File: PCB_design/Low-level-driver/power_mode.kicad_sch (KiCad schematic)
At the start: 7 parts, among them Q401 Q_NPN_EBC, Q402 Q_NPN_EBC, U401 TMUX1204DQAR

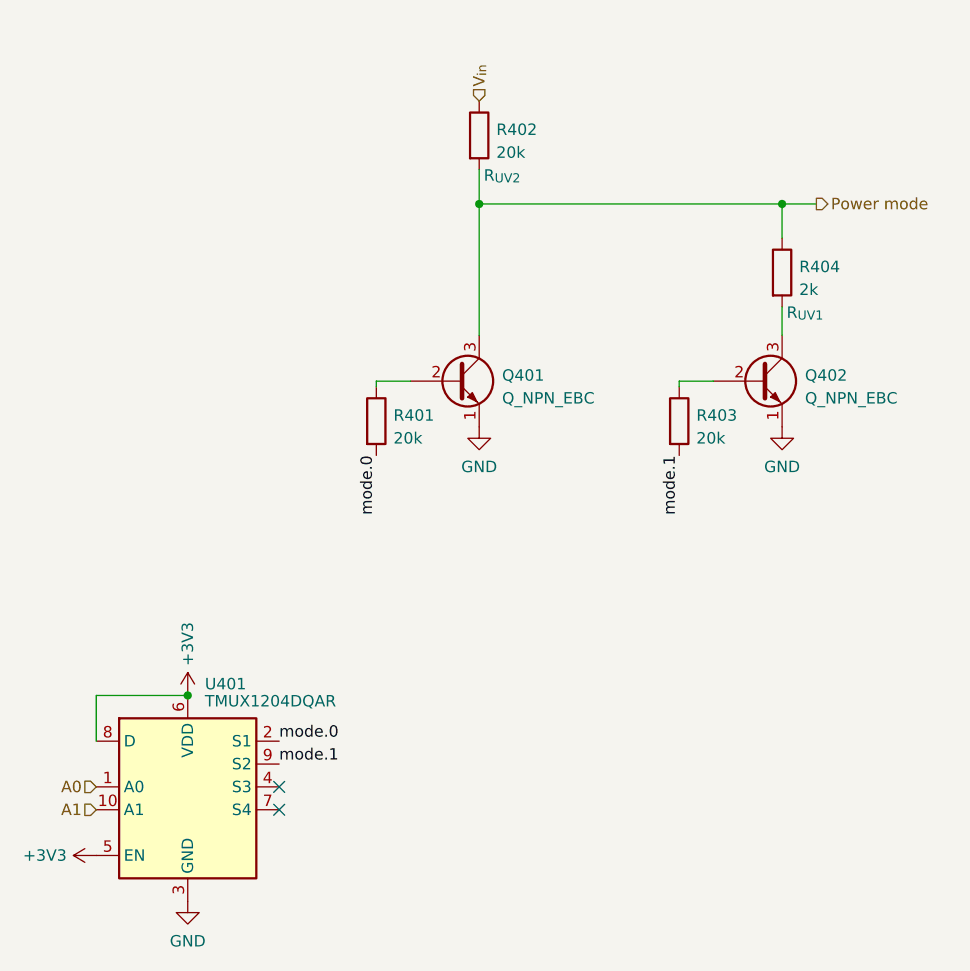
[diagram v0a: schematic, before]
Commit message: Schematic hierarchical redesign
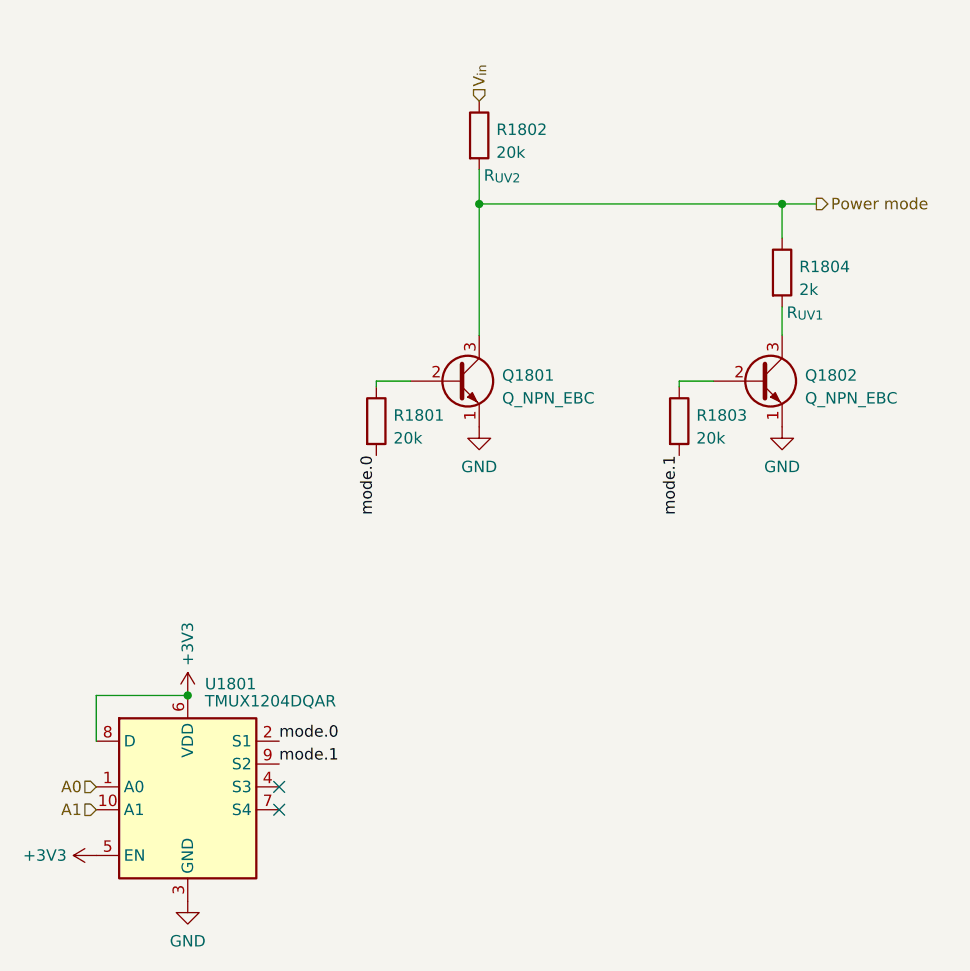
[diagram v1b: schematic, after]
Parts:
- renumbered Q401 to Q1801, Q402 to Q1802, R401 to R1801, R402 to R1802, R403 to R1803, R404 to R1804, U401 to U1801
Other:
- title: (none) -> Power supply - low level driver
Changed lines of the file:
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@@
 	(generator_version "8.0")
 	(paper "A3")
+	(title_block
+		(title "Power supply - low level driver")
+		(date "2024-06-28")
+	)
 	(junction
 		(at 118.745 68.58)
@@
 		(dnp no)
 		(fields_autoplaced yes)
-		(property "Reference" "Q402"
+		(property "Reference" "Q1802"
 			(at 154.94 87.63 0)
 			(effects
@@
 			(project "Low-level-driver"
 				(path "/2e43a8c9-1b23-4896-a481-133b23afb346/01ca3785-0e3e-4a04-8db2-6c3c91b7e708/0f5f3a01-f1db-43da-b53b-d3878d37b104"
-					(reference "Q402")
+					(reference "Q1802")
 					(unit 1)
 				)
@@
 		(on_board yes)
 		(dnp no)
-		(property "Reference" "#PWR0401"
+		(property "Reference" "#PWR01801"
 			(at 80.01 140.97 0)
 			(effects
@@
 			(project "Low-level-driver"
 				(path "/2e43a8c9-1b23-4896-a481-133b23afb346/01ca3785-0e3e-4a04-8db2-6c3c91b7e708/0f5f3a01-f1db-43da-b53b-d3878d37b104"
-					(reference "#PWR0401")
+					(reference "#PWR01801")
 					(unit 1)
 				)
@@
 		(on_board yes)
 		(dnp no)
-		(property "Reference" "R402"
+		(property "Reference" "R1802"
 			(at 120.65 60.325 0)
 			(effects
@@
 			(project "Low-level-driver"
 				(path "/2e43a8c9-1b23-4896-a481-133b23afb346/01ca3785-0e3e-4a04-8db2-6c3c91b7e708/0f5f3a01-f1db-43da-b53b-d3878d37b104"
-					(reference "R402")
+					(reference "R1802")
 					(unit 1)
 				)
@@
 		(dnp no)
 		(fields_autoplaced yes)
-		(property "Reference" "#PWR0403"
+		(property "Reference" "#PWR01803"
 			(at 86.36 152.4 0)
 			(effects
@@
 			(project "Low-level-driver"
 				(path "/2e43a8c9-1b23-4896-a481-133b23afb346/01ca3785-0e3e-4a04-8db2-6c3c91b7e708/0f5f3a01-f1db-43da-b53b-d3878d37b104"
-					(reference "#PWR0403")
+					(reference "#PWR01803")
 					(unit 1)
 				)
@@
 		(on_board yes)
 		(dnp no)
-		(property "Reference" "#PWR0402"
+		(property "Reference" "#PWR01802"
 			(at 86.36 127 0)
 			(effects
@@
 			(project "Low-level-driver"
 				(path "/2e43a8c9-1b23-4896-a481-133b23afb346/01ca3785-0e3e-4a04-8db2-6c3c91b7e708/0f5f3a01-f1db-43da-b53b-d3878d37b104"
-					(reference "#PWR0402")
+					(reference "#PWR01802")
 					(unit 1)
 				)
@@
 		(dnp no)
 		(fields_autoplaced yes)
-		(property "Reference" "Q401"
+		(property "Reference" "Q1801"
 			(at 121.285 87.63 0)
 			(effects
@@
 			(project "Low-level-driver"
 				(path "/2e43a8c9-1b23-4896-a481-133b23afb346/01ca3785-0e3e-4a04-8db2-6c3c91b7e708/0f5f3a01-f1db-43da-b53b-d3878d37b104"
-					(reference "Q401")
+					(reference "Q1801")
 					(unit 1)
 				)
@@
 		(dnp no)
 		(fields_autoplaced yes)
-		(property "Reference" "#PWR0404"
+		(property "Reference" "#PWR01804"
 			(at 118.745 99.695 0)
 			(effects
@@
 			(project "Low-level-driver"
 				(path "/2e43a8c9-1b23-4896-a481-133b23afb346/01ca3785-0e3e-4a04-8db2-6c3c91b7e708/0f5f3a01-f1db-43da-b53b-d3878d37b104"
-					(reference "#PWR0404")
+					(reference "#PWR01804")
 					(unit 1)
 				)
@@
 		(dnp no)
 		(fields_autoplaced yes)
-		(property "Reference" "#PWR0405"
+		(property "Reference" "#PWR01805"
 			(at 152.4 99.695 0)
 			(effects
@@
 			(project "Low-level-driver"
 				(path "/2e43a8c9-1b23-4896-a481-133b23afb346/01ca3785-0e3e-4a04-8db2-6c3c91b7e708/0f5f3a01-f1db-43da-b53b-d3878d37b104"
-					(reference "#PWR0405")
+					(reference "#PWR01805")
 					(unit 1)
 				)
@@
 		(dnp no)
 		(fields_autoplaced yes)
-		(property "Reference" "R401"
+		(property "Reference" "R1801"
 			(at 109.22 92.075 0)
 			(effects
@@
 			(project "Low-level-driver"
 				(path "/2e43a8c9-1b23-4896-a481-133b23afb346/01ca3785-0e3e-4a04-8db2-6c3c91b7e708/0f5f3a01-f1db-43da-b53b-d3878d37b104"
-					(reference "R401")
+					(reference "R1801")
 					(unit 1)
 				)
@@
 		(on_board yes)
 		(dnp no)
-		(property "Reference" "R404"
+		(property "Reference" "R1804"
 			(at 154.305 75.565 0)
 			(effects
@@
 			(project "Low-level-driver"
 				(path "/2e43a8c9-1b23-4896-a481-133b23afb346/01ca3785-0e3e-4a04-8db2-6c3c91b7e708/0f5f3a01-f1db-43da-b53b-d3878d37b104"
-					(reference "R404")
+					(reference "R1804")
 					(unit 1)
 				)
@@
 		(dnp no)
 		(fields_autoplaced yes)
-		(property "Reference" "R403"
+		(property "Reference" "R1803"
 			(at 142.875 92.075 0)
 			(effects
@@
 			(project "Low-level-driver"
 				(path "/2e43a8c9-1b23-4896-a481-133b23afb346/01ca3785-0e3e-4a04-8db2-6c3c91b7e708/0f5f3a01-f1db-43da-b53b-d3878d37b104"
-					(reference "R403")
+					(reference "R1803")
 					(unit 1)
 				)
@@
 		(dnp no)
 		(fields_autoplaced yes)
-		(property "Reference" "U401"
+		(property "Reference" "U1801"
 			(at 88.265 121.92 0)
 			(effects
@@
 			(project "Low-level-driver"
 				(path "/2e43a8c9-1b23-4896-a481-133b23afb346/01ca3785-0e3e-4a04-8db2-6c3c91b7e708/0f5f3a01-f1db-43da-b53b-d3878d37b104"
-					(reference "U401")
-					(unit 1)
-				)
+					(reference "U1801")
+					(unit 1)
+				)
